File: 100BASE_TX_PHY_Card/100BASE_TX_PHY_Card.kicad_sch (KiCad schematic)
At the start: 54 parts, among them J1 Conn_02x11_Odd_Even, J2 RJ45_Amphenol_RJMG1BD3B8K1ANR, SW1 SW_DIP_x07, U1 LAN8710A, Y1 25M

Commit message: LAN8710A PHY Card 4layer design
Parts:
- removed C1, C2: 30p, Capacitor_SMD:C_0402_1005Metric, symbol Device:C
- removed C10, C11, C12, C13, C9: dnp, Capacitor_SMD:C_0402_1005Metric, symbol Device:C
- removed C3, C4, C5: 100n, Capacitor_SMD:C_0402_1005Metric, symbol Device:C
- removed C6: 4,7u, Capacitor_SMD:C_0402_1005Metric, symbol Device:C
- removed C7: 470p, Capacitor_SMD:C_0402_1005Metric, symbol Device:C
- removed C8: 1u, Capacitor_SMD:C_0402_1005Metric, symbol Device:C
- removed FB1: FerriteBead, Resistor_SMD:R_0201_0603Metric, symbol Device:FerriteBead
- removed J1: Conn_02x11_Odd_Even, Connector_PinHeader_2.54mm:PinHeader_2x11_P2.54mm_Horizontal, symbol Connector_Generic:Conn_02x11_Odd_Even
- removed J2: RJ45_Amphenol_RJMG1BD3B8K1ANR, Connector_RJ:RJ45_Amphenol_RJMG1BD3B8K1ANR, symbol Connector:RJ45_Amphenol_RJMG1BD3B8K1ANR
- removed R1, R2, R3, R4, R5, R6, R7, R8: 22, Resistor_SMD:R_0402_1005Metric, symbol Device:R
- removed R10, R11, R12, R13, R14, R15, R9: 1k, Resistor_SMD:R_0402_1005Metric, symbol Device:R
- removed R16, R17, R18, R19, R20, R21, R22: 10k, Resistor_SMD:R_0402_1005Metric, symbol Device:R
- removed R23: 1M, Resistor_SMD:R_0402_1005Metric, symbol Device:R
- removed R24, R30: 2,49k, Resistor_SMD:R_0402_1005Metric, symbol Device:R
- removed R25, R26, R27, R28: 49,9, Resistor_SMD:R_0402_1005Metric, symbol Device:R
- removed R29: 0, Resistor_SMD:R_0402_1005Metric, symbol Device:R
- removed R31: 12.1k, Resistor_SMD:R_0402_1005Metric, symbol Device:R
- removed R32, R33: R, Resistor_SMD:R_0402_1005Metric, symbol Device:R
- removed R34, R35: 330, Resistor_SMD:R_0402_1005Metric, symbol Device:R
- removed SW1: SW_DIP_x07, Button_Switch_SMD:SW_DIP_SPSTx07_Slide_KingTek_DSHP07TJ_W5.25mm_P1.27mm_JPin, symbol Switch:SW_DIP_x07
- removed U1: LAN8710A, Package_DFN_QFN:QFN-32-1EP_5x5mm_P0.5mm_EP3.3x3.3mm_ThermalVias, symbol Interface_Ethernet:LAN8710A
- removed Y1: 25M, Crystal:Crystal_SMD_0603-4Pin_6.0x3.5mm, symbol Device:Crystal
- added C1: 470pF 0603, 0603_CAP, symbol PHY_PCB-altium-import:root_1_Cap
- added C10: 15pF 0603, 0603_CAP, symbol PHY_PCB-altium-import:root_1_Cap
- added C2: 1uF 0603, 0603_CAP, symbol PHY_PCB-altium-import:root_1_Cap
- added C3, C4, C5, C7, C8: 100nF 0603, 0603_CAP, symbol PHY_PCB-altium-import:root_1_Cap
- added C6: 10uF 1206, 1206_CAP, symbol PHY_PCB-altium-import:root_1_Cap
- added C9: 10nF, 1206_CAP, symbol PHY_PCB-altium-import:root_1_Cap
- added L1, L2: Ferrite bead 120R/100MHz, 0603_IND, symbol PHY_PCB-altium-import:root_0_Inductor
- added P1: RJMG1BD3B8K1ANR, RJMG1BD3B8K1ANR, symbol PHY_PCB-altium-import:root_0_RJ45_RJMG1BD3B8K1ANR
- added R1: 12k1 0603, 0603, symbol PHY_PCB-altium-import:root_0_Res2
- added R10, R7, R8, R9: 49R9 0603, 0603, symbol PHY_PCB-altium-import:root_1_Res2
- added R2: 100k 0603, 0603, symbol PHY_PCB-altium-import:root_3_Res2
- added R3: 1M 1206, 1206, symbol PHY_PCB-altium-import:root_3_Res2
- added R4, R6: 330R 0603, 0603, symbol PHY_PCB-altium-import:root_0_Res2
- added U1: LAN8710A, LAN8710A, symbol PHY_PCB-altium-import:root_0_LAN8710A
- added Y1: 25MHz 3225, XTAL_3225, symbol PHY_PCB-altium-import:root_0_mirrored_XTAL
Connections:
- net CRS: now also U1.14 (CRS)
- net GND: now also C1.1, C10.1, C2.1, C3.1, C4.1, C5.1, C6.1, C7.1, C8.1, C9.1, P1.8 (GND), R1.2, R3.2, R6.2, U1.0 (VSS), Y1.2 (GND)
- net LED1: now also P1.L4 (GREEN+), U1.3 (LED1/REGOFF)
- net LED2: now also U1.2 (LED2/nINTSEL)
- net MDC: now also U1.17 (MDC)
- net MDIO: now also U1.16 (MDIO)
- net PHY_IRQ: now also U1.18 (nINT/TXER/TXD4)
- net RXDV: now also U1.26 (RXDV)
- net TXCLK: now also U1.20 (TXCLK)
- net TXD0: now also U1.22 (TXD0)
- net TXD1: now also U1.23 (TXD1)
- net TXD2: now also U1.24 (TXD2)
- net TXD3: now also U1.25 (TXD3)
- net TXEN: now also U1.21 (TXEN)
- net VDDCR: now also C1.2, C2.2, U1.6 (VDDCR)
- new net: P1.L3 (GREEN-), R6.1
- new net: P1.L2 (YELLOW-), R4.1
- new net: R1.1, U1.32 (RBIAS)
- new net: U1.5 (XTAL1/CLKIN), Y1.3 (Out)
- new net /MODE0: U1.11 (RXD0/MODE0)
- new net /MODE1: U1.10 (RXD1/MODE1)
- new net /MODE2: U1.15 (COL/CRS_DV/MODE2)
- new net /PHYAD0: U1.13 (RXER/RXD4/PHYAD0)
- new net /PHYAD1: U1.7 (RXCLK/PHYAD1)
- new net /PHYAD2: U1.8 (RXD3/PHYAD2)
- new net /RMIISEL: U1.9 (RXD2/RMIISEL)
- new net LED2+: P1.L1 (YELLOW+)
- new net LED2-: R4.2
- new net PHY_RST: C7.2, R2.1, U1.19 (nRST)
- new net RX_n: P1.6 (RD-), R10.2, U1.30 (RXN)
- new net RX_p: P1.3 (RD+), R9.2, U1.31 (RXP)
- new net SHIELD: C9.2, P1.S (SHIELD), R3.1
- new net TX_n: P1.2 (TD-), R8.2, U1.28 (TXN)
- new net TX_p: P1.1 (TD+), R7.2, U1.29 (TXP)
- new net VCC_3V3: L1.2, L2.2, R2.2
- new net VDDIO: C5.2, C6.2, C8.2, L2.1, U1.12 (VDDIO), Y1.4 (VCC)
- new net VDD_A: C10.2, C3.2, C4.2, L1.1, P1.4 (TCT), P1.5 (RCT), R10.1, R7.1, R8.1, R9.1, U1.1 (VDD2A), U1.27 (VDD1A)
- no-connect marks 0 -> 1
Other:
- added sheet Untitled Sheet (untitled.kicad_sch)

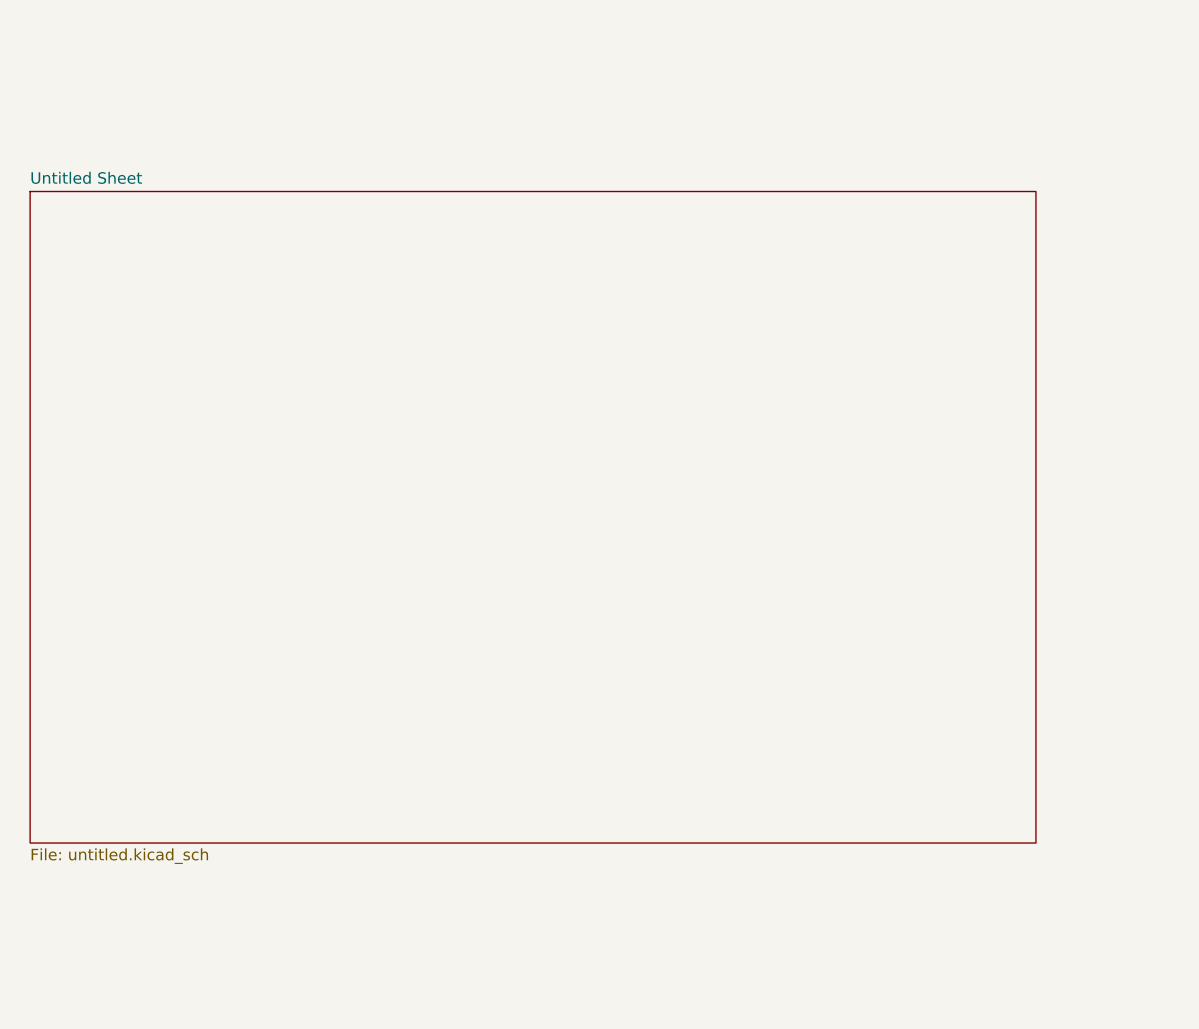
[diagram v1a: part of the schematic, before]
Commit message: Added missing Connectors schematic
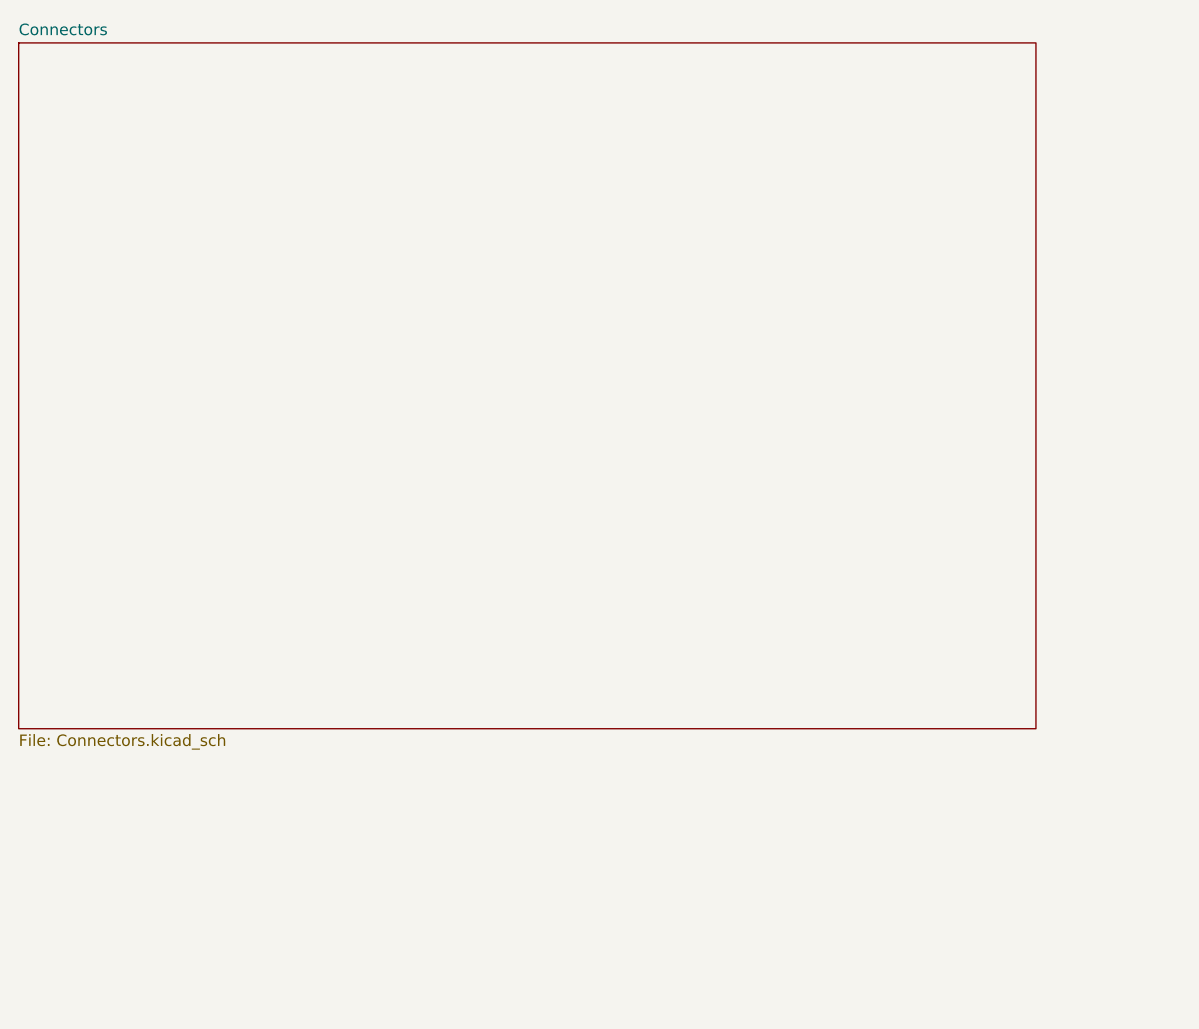
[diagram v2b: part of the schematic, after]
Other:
- removed sheet Untitled Sheet
- added sheet Connectors (Connectors.kicad_sch)
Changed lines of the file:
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@@
 	)
 	(sheet
-		(at -115.57 24.13)
-		(size 111.76 72.39)
+		(at -116.84 7.62)
+		(size 113.03 76.2)
 		(fields_autoplaced yes)
 		(stroke
@@
 			(color 0 0 0 0.0000)
 		)
-		(property "Sheetname" "Untitled Sheet"
-			(at -115.57 23.4184 0)
+		(property "Sheetname" "Connectors"
+			(at -116.84 6.9084 0)
 			(effects
 				(font
@@
 			)
 		)
-		(property "Sheetfile" "untitled.kicad_sch"
-			(at -115.57 97.1046 0)
+		(property "Sheetfile" "Connectors.kicad_sch"
+			(at -116.84 84.4046 0)
 			(effects
 				(font
@@
 			)
 		)
+		(property "Field2" ""
+			(at -116.84 7.62 0)
+			(effects
+				(font
+					(size 1.27 1.27)
+				)
+				(hide yes)
+			)
+		)
 		(instances
-			(project "PHY_PCB"
+			(project "100BASE_TX_PHY_Card"
 				(path "/f8be191c-0b80-48bc-9689-d2851ae31544"
 					(page "2")
